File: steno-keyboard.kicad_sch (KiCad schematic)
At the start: 51 parts, among them SW1 SW_Push, SW10 SW_Push, SW11 SW_Push, SW12 SW_Push, SW13 SW_Push, SW14 SW_Push, SW15 SW_Push, SW16 SW_Push, SW17 SW_Push, SW18 SW_Push, SW19 SW_Push, SW2 SW_Push, SW20 SW_Push, SW21 SW_Push, SW22 SW_Push, SW23 SW_Push, SW24 SW_Push, SW25 SW_Push, SW3 SW_Push, SW4 SW_Push, SW5 SW_Push, SW6 SW_Push, SW7 SW_Push, SW8 SW_Push, SW9 SW_Push

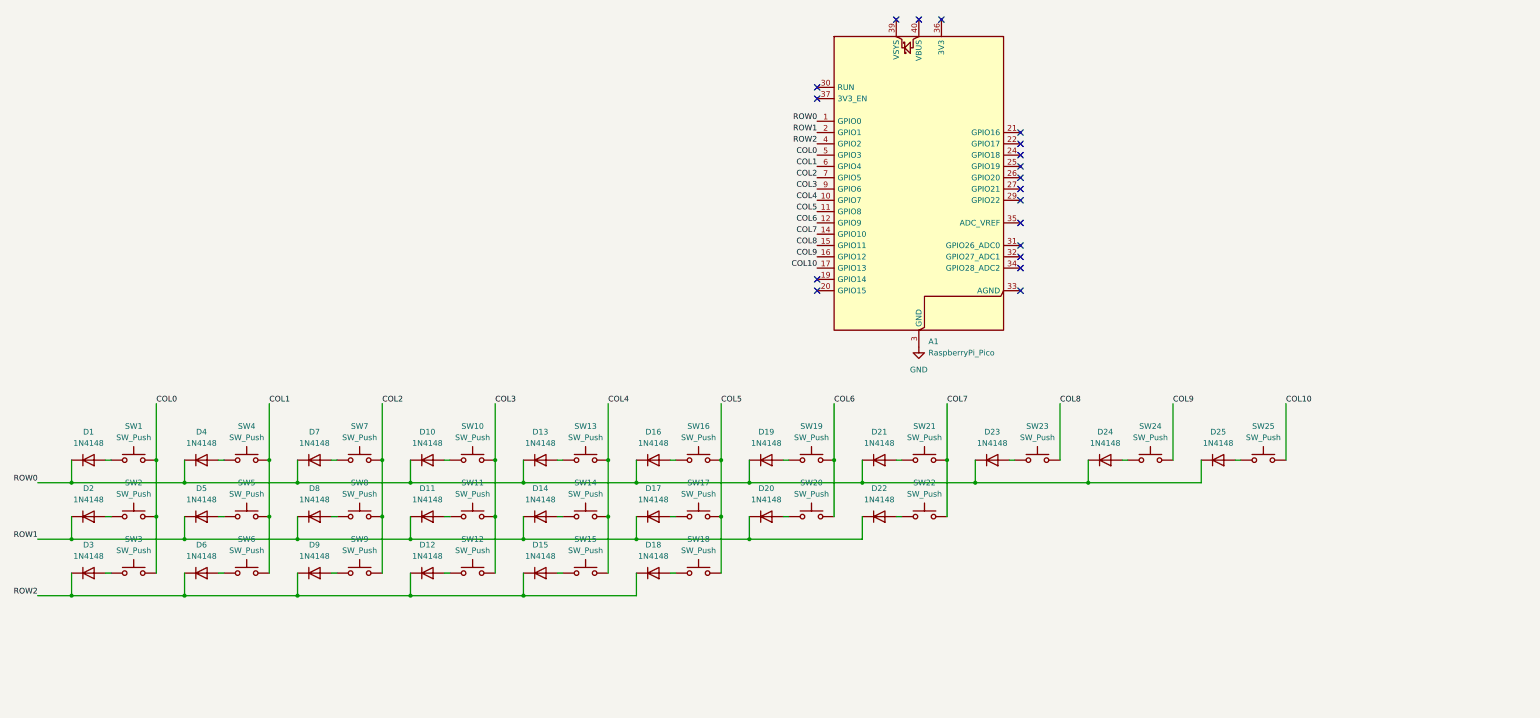
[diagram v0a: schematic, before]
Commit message: Update steno-keyboard.kicad_sch
Changed layout from matrix to direct pin into pico
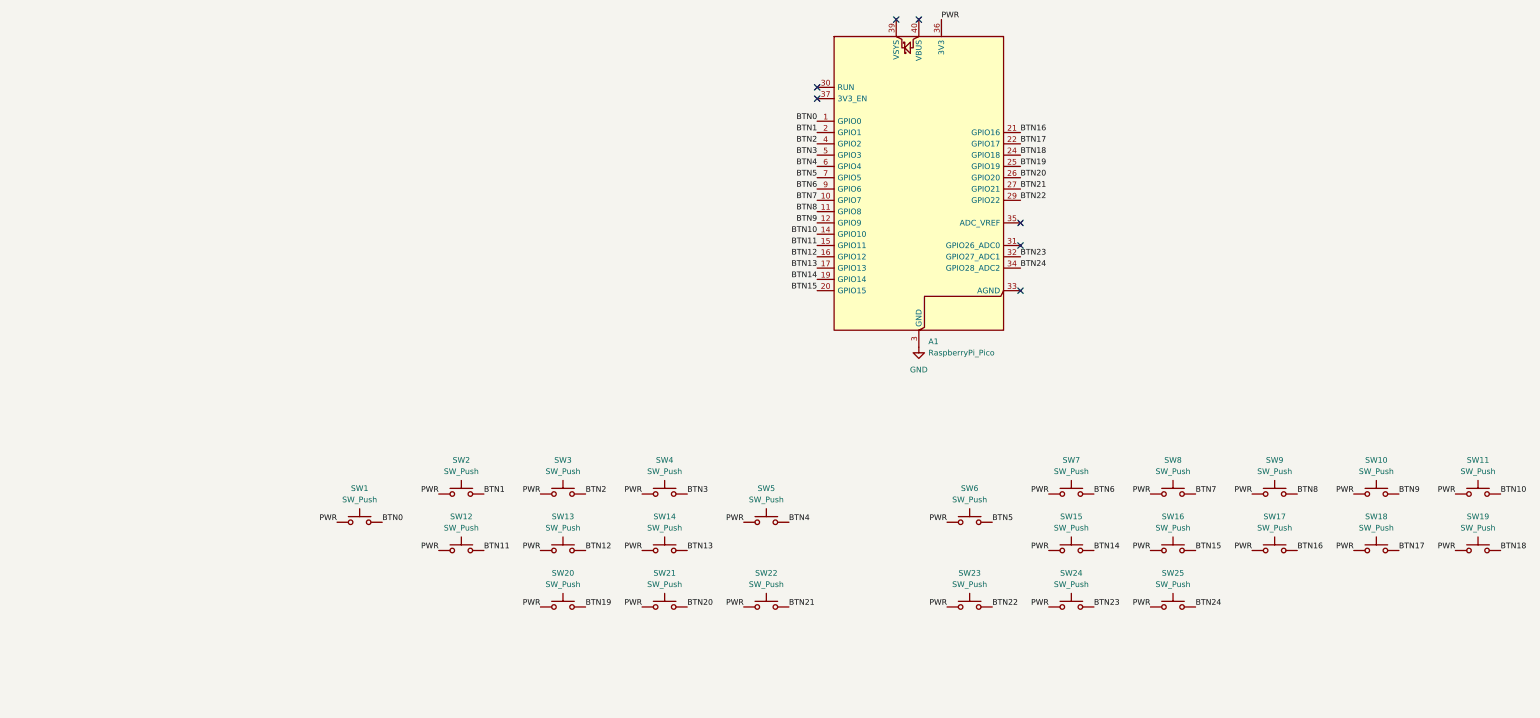
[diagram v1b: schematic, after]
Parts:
- removed D1, D10, D11, D12, D13, D14, D15, D16, D17, D18, D19, D2, D20, D21, D22, D23, D24, D25, D3, D4, D5, D6, D7, D8, D9: 1N4148, Diode_THT:D_DO-35_SOD27_P7.62mm_Horizontal, symbol Diode:1N4148
- SW1, SW10, SW11, SW12, SW13, SW14, SW15, SW16, SW17, SW18, SW19, SW2, SW20, SW21, SW22, SW23, SW24, SW25, SW3, SW4, SW5, SW6, SW7, SW8, SW9: footprint MX_Only:MXOnly-1U -> (none)
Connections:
- net ROW0 is gone; now on net BTN0: A1.1 (GPIO0)
- net ROW1 is gone; now on net BTN1: A1.2 (GPIO1)
- net ROW2 is gone; now on net BTN2: A1.4 (GPIO2)
- net BTN15: now reaches SW16.2
- net BTN15: now also A1.20 (GPIO15)
- net BTN10: now reaches SW11.2
- net BTN10: now also A1.14 (GPIO10)
- net BTN14: now reaches SW15.2
- net BTN14: now also A1.19 (GPIO14)
- net BTN7: now reaches SW8.2
- net BTN7: now also A1.10 (GPIO7)
- net BTN21: now reaches SW22.2
- net BTN21: now also A1.27 (GPIO21)
- net BTN4: now reaches SW5.2
- net BTN4: now also A1.6 (GPIO4)
- net BTN2: now reaches SW3.2
- net BTN0: now reaches SW1.2
- net BTN18: now reaches SW19.2
- net BTN18: now also A1.24 (GPIO18)
- net BTN16: now reaches A1.21 (GPIO16)
- net BTN16: now also SW17.2
- net BTN17: now reaches A1.22 (GPIO17)
- net BTN17: now also SW18.2
- net BTN19: now reaches A1.25 (GPIO19)
- net BTN19: now also SW20.2
- net BTN20: now reaches A1.26 (GPIO20)
- net BTN20: now also SW21.2
- net BTN22: now reaches A1.29 (GPIO22)
- net BTN22: now also SW23.2
- net BTN23: now reaches A1.32 (GPIO27_ADC1)
- net BTN23: now also SW24.2
- net BTN24: now reaches A1.34 (GPIO28_ADC2)
- net BTN24: now also SW25.2
- net PWR: now reaches A1.36 (3V3)
- net PWR: now also SW1.1, SW10.1, SW11.1, SW12.1, SW13.1, SW14.1, SW15.1, SW16.1, SW17.1, SW18.1, SW19.1, SW2.1, SW20.1, SW21.1, SW22.1, SW23.1, SW24.1, SW25.1, SW3.1, SW4.1, SW5.1, SW6.1, SW7.1, SW8.1, SW9.1
- net BTN11: now reaches SW12.2
- net BTN11: now also A1.15 (GPIO11)
- net BTN6: now reaches SW7.2
- net BTN6: now also A1.9 (GPIO6)
- net BTN13: now reaches SW14.2
- net BTN13: now also A1.17 (GPIO13)
- net BTN12: now reaches SW13.2
- net BTN12: now also A1.16 (GPIO12)
- net BTN8: now reaches SW9.2
- net BTN8: now also A1.11 (GPIO8)
- net BTN5: now reaches SW6.2
- net BTN5: now also A1.7 (GPIO5)
- net BTN1: now reaches SW2.2
- net BTN9: now reaches SW10.2
- net BTN9: now also A1.12 (GPIO9)
- net BTN3: now reaches SW4.2
- net BTN3: now also A1.5 (GPIO3)
- removed net COL0: A1.5 (GPIO3), SW1.1, SW2.1, SW3.1
- removed net COL1: A1.6 (GPIO4), SW4.1, SW5.1, SW6.1
- removed net COL10: A1.17 (GPIO13), SW25.1
- removed net COL2: A1.7 (GPIO5), SW7.1, SW8.1, SW9.1
- removed net COL3: A1.9 (GPIO6), SW10.1, SW11.1, SW12.1
- removed net COL4: A1.10 (GPIO7), SW13.1, SW14.1, SW15.1
- removed net COL5: A1.11 (GPIO8), SW16.1, SW17.1, SW18.1
- removed net COL6: A1.12 (GPIO9), SW19.1, SW20.1
- removed net COL7: A1.14 (GPIO10), SW21.1, SW22.1
- removed net COL8: A1.15 (GPIO11), SW23.1
- removed net COL9: A1.16 (GPIO12), SW24.1
- no-connect marks 19 -> 7

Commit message: Updated PCB and footprints
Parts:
- SW1, SW10, SW11, SW12, SW13, SW14, SW15, SW16, SW17, SW18, SW19, SW2, SW20, SW21, SW22, SW23, SW24, SW25, SW3, SW4, SW5, SW6, SW7, SW8, SW9: footprint (none) -> MX_Solderable:MX-Solderable-1U
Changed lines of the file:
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@@
 			)
 		)
-		(property "Footprint" ""
+		(property "Footprint" "MX_Solderable:MX-Solderable-1U"
 			(at 370.84 134.62 0)
 			(effects
@@
 			)
 		)
-		(property "Footprint" ""
+		(property "Footprint" "MX_Solderable:MX-Solderable-1U"
 			(at 256.54 128.27 0)
 			(effects
@@
 			)
 		)
-		(property "Footprint" ""
+		(property "Footprint" "MX_Solderable:MX-Solderable-1U"
 			(at 347.98 134.62 0)
 			(effects
@@
 			)
 		)
-		(property "Footprint" ""
+		(property "Footprint" "MX_Solderable:MX-Solderable-1U"
 			(at 347.98 121.92 0)
 			(effects
@@
 			)
 		)
-		(property "Footprint" ""
+		(property "Footprint" "MX_Solderable:MX-Solderable-1U"
 			(at 165.1 121.92 0)
 			(effects
@@
 			)
 		)
-		(property "Footprint" ""
+		(property "Footprint" "MX_Solderable:MX-Solderable-1U"
 			(at 142.24 121.92 0)
 			(effects
@@
 			)
 		)
-		(property "Footprint" ""
+		(property "Footprint" "MX_Solderable:MX-Solderable-1U"
 			(at 302.26 134.62 0)
 			(effects
@@
 			)
 		)
-		(property "Footprint" ""
+		(property "Footprint" "MX_Solderable:MX-Solderable-1U"
 			(at 187.96 147.32 0)
 			(effects
@@
 			)
 		)
-		(property "Footprint" ""
+		(property "Footprint" "MX_Solderable:MX-Solderable-1U"
 			(at 302.26 121.92 0)
 			(effects
@@
 			)
 		)
-		(property "Footprint" ""
+		(property "Footprint" "MX_Solderable:MX-Solderable-1U"
 			(at 279.4 147.32 0)
 			(effects
@@
 			)
 		)
-		(property "Footprint" ""
+		(property "Footprint" "MX_Solderable:MX-Solderable-1U"
 			(at 279.4 121.92 0)
 			(effects
@@
 			)
 		)
-		(property "Footprint" ""
+		(property "Footprint" "MX_Solderable:MX-Solderable-1U"
 			(at 302.26 147.32 0)
 			(effects
@@
 			)
 		)
-		(property "Footprint" ""
+		(property "Footprint" "MX_Solderable:MX-Solderable-1U"
 			(at 210.82 128.27 0)
 			(effects
@@
 			)
 		)
-		(property "Footprint" ""
+		(property "Footprint" "MX_Solderable:MX-Solderable-1U"
 			(at 325.12 134.62 0)
 			(effects
@@
 			)
 		)
-		(property "Footprint" ""
+		(property "Footprint" "MX_Solderable:MX-Solderable-1U"
 			(at 187.96 121.92 0)
 			(effects
@@
 			)
 		)
-		(property "Footprint" ""
+		(property "Footprint" "MX_Solderable:MX-Solderable-1U"
 			(at 165.1 134.62 0)
 			(effects
@@
 			)
 		)
-		(property "Footprint" ""
+		(property "Footprint" "MX_Solderable:MX-Solderable-1U"
 			(at 119.38 128.27 0)
 			(effects
@@
 			)
 		)
-		(property "Footprint" ""
+		(property "Footprint" "MX_Solderable:MX-Solderable-1U"
 			(at 210.82 147.32 0)
 			(effects
@@
 			)
 		)
-		(property "Footprint" ""
+		(property "Footprint" "MX_Solderable:MX-Solderable-1U"
 			(at 142.24 134.62 0)
 			(effects
@@
 			)
 		)
-		(property "Footprint" ""
+		(property "Footprint" "MX_Solderable:MX-Solderable-1U"
 			(at 279.4 134.62 0)
 			(effects
@@
 			)
 		)
-		(property "Footprint" ""
+		(property "Footprint" "MX_Solderable:MX-Solderable-1U"
 			(at 165.1 147.32 0)
 			(effects
@@
 			)
 		)
-		(property "Footprint" ""
+		(property "Footprint" "MX_Solderable:MX-Solderable-1U"
 			(at 187.96 134.62 0)
 			(effects
@@
 			)
 		)
-		(property "Footprint" ""
+		(property "Footprint" "MX_Solderable:MX-Solderable-1U"
 			(at 325.12 121.92 0)
 			(effects
@@
 			)
 		)
-		(property "Footprint" ""
+		(property "Footprint" "MX_Solderable:MX-Solderable-1U"
 			(at 370.84 121.92 0)
 			(effects
@@
 			)
 		)
-		(property "Footprint" ""
+		(property "Footprint" "MX_Solderable:MX-Solderable-1U"
 			(at 256.54 147.32 0)
 			(effects

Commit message: Finished PCB and rerouted some wires
Although the layout is messy, it allows for clean routing of the GPIOs
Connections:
- net BTN10: now also A1.34 (GPIO28_ADC2); no longer A1.14 (GPIO10)
- net BTN11: now also A1.7 (GPIO5); no longer A1.15 (GPIO11)
- net BTN12: now also A1.9 (GPIO6); no longer A1.16 (GPIO12)
- net BTN13: now also A1.10 (GPIO7); no longer A1.17 (GPIO13)
- net BTN14: now also A1.24 (GPIO18); no longer A1.19 (GPIO14)
- net BTN15: now also A1.22 (GPIO17); no longer A1.20 (GPIO15)
- net BTN17: now also A1.20 (GPIO15); no longer A1.22 (GPIO17)
- net BTN18: now also A1.19 (GPIO14); no longer A1.24 (GPIO18)
- net BTN19: now also A1.11 (GPIO8); no longer A1.25 (GPIO19)
- net BTN20: now also A1.12 (GPIO9); no longer A1.26 (GPIO20)
- net BTN21: now also A1.14 (GPIO10); no longer A1.27 (GPIO21)
- net BTN22: now also A1.15 (GPIO11); no longer A1.29 (GPIO22)
- net BTN23: now also A1.16 (GPIO12); no longer A1.32 (GPIO27_ADC1)
- net BTN24: now also A1.17 (GPIO13); no longer A1.34 (GPIO28_ADC2)
- net BTN5: now also A1.25 (GPIO19); no longer A1.7 (GPIO5)
- net BTN6: now also A1.26 (GPIO20); no longer A1.9 (GPIO6)
- net BTN7: now also A1.27 (GPIO21); no longer A1.10 (GPIO7)
- net BTN8: now also A1.29 (GPIO22); no longer A1.11 (GPIO8)
- net BTN9: now also A1.32 (GPIO27_ADC1); no longer A1.12 (GPIO9)
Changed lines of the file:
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@@
 		)
 	)
-	(label "BTN12"
+	(label "BTN23"
 		(at 222.25 73.66 180)
 		(effects
@@
 		)
 	)
-	(label "BTN5"
+	(label "BTN11"
 		(at 222.25 55.88 180)
 		(effects
@@
 		)
 	)
-	(label "BTN10"
+	(label "BTN21"
 		(at 222.25 68.58 180)
 		(effects
@@
 		)
 	)
-	(label "BTN19"
+	(label "BTN5"
 		(at 267.97 53.34 0)
 		(effects
@@
 		)
 	)
-	(label "BTN6"
+	(label "BTN12"
 		(at 222.25 58.42 180)
 		(effects
@@
 		)
 	)
-	(label "BTN13"
+	(label "BTN24"
 		(at 222.25 76.2 180)
 		(effects
@@
 		)
 	)
-	(label "BTN8"
+	(label "BTN19"
 		(at 222.25 63.5 180)
 		(effects
@@
 		)
 	)
-	(label "BTN20"
+	(label "BTN6"
 		(at 267.97 55.88 0)
 		(effects
@@
 		)
 	)
-	(label "BTN14"
+	(label "BTN18"
 		(at 222.25 78.74 180)
 		(effects
@@
 		)
 	)
-	(label "BTN24"
+	(label "BTN10"
 		(at 267.97 76.2 0)
 		(effects
@@
 		)
 	)
-	(label "BTN18"
+	(label "BTN14"
 		(at 267.97 50.8 0)
 		(effects
@@
 		)
 	)
-	(label "BTN21"
+	(label "BTN7"
 		(at 267.97 58.42 0)
 		(effects
@@
 		)
 	)
-	(label "BTN22"
+	(label "BTN8"
 		(at 267.97 60.96 0)
 		(effects
@@
 		)
 	)
-	(label "BTN15"
+	(label "BTN17"
 		(at 222.25 81.28 180)
 		(effects
@@
 		)
 	)
-	(label "BTN23"
+	(label "BTN9"
 		(at 267.97 73.66 0)
 		(effects
@@
 		)
 	)
-	(label "BTN7"
+	(label "BTN13"
 		(at 222.25 60.96 180)
 		(effects
@@
 		)
 	)
-	(label "BTN11"
+	(label "BTN22"
 		(at 222.25 71.12 180)
 		(effects
@@
 		)
 	)
-	(label "BTN9"
+	(label "BTN20"
 		(at 222.25 66.04 180)
 		(effects
@@
 		)
 	)
-	(label "BTN17"
+	(label "BTN15"
 		(at 267.97 48.26 0)
 		(effects

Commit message: Finished PCB
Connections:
- net GND: now also A1.33 (AGND), SW1.1, SW10.1, SW11.1, SW12.1, SW13.1, SW14.1, SW15.1, SW16.1, SW17.1, SW18.1, SW19.1, SW2.1, SW20.1, SW21.1, SW22.1, SW23.1, SW24.1, SW25.1, SW3.1, SW4.1, SW5.1, SW6.1, SW7.1, SW8.1, SW9.1
- removed net PWR: A1.36 (3V3), SW1.1, SW10.1, SW11.1, SW12.1, SW13.1, SW14.1, SW15.1, SW16.1, SW17.1, SW18.1, SW19.1, SW2.1, SW20.1, SW21.1, SW22.1, SW23.1, SW24.1, SW25.1, SW3.1, SW4.1, SW5.1, SW6.1, SW7.1, SW8.1, SW9.1
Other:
- moved on the sheet: SW10, SW11, SW15, SW16, SW17, SW18, SW19, SW23, SW24, SW25, SW6, SW7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
